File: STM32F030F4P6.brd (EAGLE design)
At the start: 17.8 x 27.9 mm, 11 parts, among them J3 455-1750-1-ND, U1 STM32F030F4P6, U2 CJA1117B-3.3-SOT89

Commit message: Made inline.
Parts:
- moved J2 26.2 mm to (2.54, 2.54), turned to 90 degrees
- moved J1 25.4 mm to (2.54, 50.8)
- moved U1 12.7 mm to (8.89, 26.7), turned to 270 degrees
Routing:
- net SWCLK: track 11.4 -> 0.00 mm
- net BOOT0: track 11.4 -> 0.00 mm
- net A5: track 11.4 -> 0.00 mm
- net A4: track 11.4 -> 0.00 mm
- net SWDIO: track 9.25 -> 0.00 mm
- net A6: track 9.25 -> 0.00 mm
- net OSC_IN: track 9.25 -> 0.00 mm
- net A3: track 9.25 -> 0.00 mm
- net OSC_OUT: track 7.36 -> 0.00 mm
- net A2: track 7.36 -> 0.00 mm
- net A7: track 7.29 -> 0.00 mm
- net A10: track 7.29 -> 0.00 mm
- net NRST: track 5.40 -> 0.00 mm
- net A1: track 5.40 -> 0.00 mm
- net A9: track 5.03 -> 0.00 mm
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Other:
- board size 17.8 x 27.9 mm -> 17.8 x 53.3 mm

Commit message: Added capacitors, resistors, diodes, LEDs, and J-Link connector.
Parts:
- added C2, C3, C4, C5, C6, C7: (no value), adafruit:C0603
- added D2: (no value), adafruit:SOD-123
- added J4: CORTEX_DEBUG_MINIMUM_PTH, SparkFun-Connectors:2X5-PTH-1.27MM
- added LED2: (no value), adafruit:CHIPLED_0603
- added R2, R3, R4, R5: (no value), adafruit:R0603
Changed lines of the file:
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@@
 <attribute name="VALUE" x="4.572" y="1.27" size="0.6096" layer="27" font="vector" ratio="20" rot="R90"/>
+</element>
+<element name="R2" library="adafruit" package="R0603" value="" x="-36.83" y="-3.81" smashed="yes">
+<attribute name="NAME" x="-37.719" y="-2.921" size="1.27" layer="25"/>
+<attribute name="VALUE" x="-37.719" y="-5.842" size="1.27" layer="27"/>
+</element>
+<element name="R3" library="adafruit" package="R0603" value="" x="-36.83" y="-7.62" smashed="yes">
+<attribute name="NAME" x="-37.719" y="-6.731" size="1.27" layer="25"/>
+<attribute name="VALUE" x="-37.719" y="-9.652" size="1.27" layer="27"/>
+</element>
+<element name="R4" library="adafruit" package="R0603" value="" x="-36.83" y="-11.43" smashed="yes">
+<attribute name="NAME" x="-37.719" y="-10.541" size="1.27" layer="25"/>
+<attribute name="VALUE" x="-37.719" y="-13.462" size="1.27" layer="27"/>
+</element>
+<element name="R5" library="adafruit" package="R0603" value="" x="-36.83" y="-15.24" smashed="yes">
+<attribute name="NAME" x="-37.719" y="-14.351" size="1.27" layer="25"/>
+<attribute name="VALUE" x="-37.719" y="-17.272" size="1.27" layer="27"/>
+</element>
+<element name="C2" library="adafruit" package="C0603" value="" x="-36.83" y="-19.05" smashed="yes">
+<attribute name="NAME" x="-37.719" y="-18.288" size="1.27" layer="25"/>
+<attribute name="VALUE" x="-37.719" y="-21.082" size="1.27" layer="27"/>
+</element>
+<element name="C3" library="adafruit" package="C0603" value="" x="-36.83" y="-22.86" smashed="yes">
+<attribute name="NAME" x="-37.719" y="-22.098" size="1.27" layer="25"/>
+<attribute name="VALUE" x="-37.719" y="-24.892" size="1.27" layer="27"/>
+</element>
+<element name="C4" library="adafruit" package="C0603" value="" x="-36.83" y="-26.67" smashed="yes">
+<attribute name="NAME" x="-37.719" y="-25.908" size="1.27" layer="25"/>
+<attribute name="VALUE" x="-37.719" y="-28.702" size="1.27" layer="27"/>
+</element>
+<element name="C5" library="adafruit" package="C0603" value="" x="-36.83" y="-30.48" smashed="yes">
+<attribute name="NAME" x="-37.719" y="-29.718" size="1.27" layer="25"/>
+<attribute name="VALUE" x="-37.719" y="-32.512" size="1.27" layer="27"/>
+</element>
+<element name="C6" library="adafruit" package="C0603" value="" x="-36.83" y="-34.29" smashed="yes">
+<attribute name="NAME" x="-37.719" y="-33.528" size="1.27" layer="25"/>
+<attribute name="VALUE" x="-37.719" y="-36.322" size="1.27" layer="27"/>
+</element>
+<element name="C7" library="adafruit" package="C0603" value="" x="-36.83" y="-38.1" smashed="yes">
+<attribute name="NAME" x="-37.719" y="-37.338" size="1.27" layer="25"/>
+<attribute name="VALUE" x="-37.719" y="-40.132" size="1.27" layer="27"/>
+</element>
+<element name="LED2" library="adafruit" package="CHIPLED_0603" value="" x="-36.83" y="-43.18" smashed="yes">
+<attribute name="NAME" x="-37.465" y="-44.45" size="1.27" layer="25" rot="R90"/>
+<attribute name="VALUE" x="-34.925" y="-44.45" size="1.27" layer="27" rot="R90"/>
+</element>
+<element name="D2" library="adafruit" package="SOD-123" value="" x="-35.56" y="-46.99" smashed="yes">
+<attribute name="NAME" x="-36.66" y="-45.99" size="0.4064" layer="25"/>
+<attribute name="VALUE" x="-36.66" y="-48.274" size="0.4064" layer="27"/>
+</element>
+<element name="J4" library="SparkFun-Connectors" package="2X5-PTH-1.27MM" value="CORTEX_DEBUG_MINIMUM_PTH" x="-35.56" y="-52.07" smashed="yes">
+<attribute name="NAME" x="-37.1348" y="-50.1396" size="0.6096" layer="25" font="vector" ratio="20"/>
+<attribute name="VALUE" x="-37.3888" y="-54.5338" size="0.6096" layer="27" font="vector" ratio="20"/>
 </element>
 </elements>

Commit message: Connected all components.
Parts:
- added C8: (no value), adafruit:C0603
- added FRAME1: FRAME-LETTER, SparkFun-Aesthetics:CREATIVE_COMMONS
- added J5: (no value), SparkFun-Connectors:1X02
- J1: device SparkFun-Connectors:1X10 -> SparkFun-Connectors:1X11
- moved J2 22.9 mm to (2.54, 25.4), turned to 270 degrees
- moved J1 2.54 mm to (2.54, 53.3)
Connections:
- new net N$1: J3.2, R1.1
- new net N$3: C6.1, R2.1, Y1.P$1
- new net N$5: D2.A, U2.2, U2.4
- new net N$7: LED1.C, R3.2
- new net N$8: LED2.C, R4.1
- new net VIN_2.4-3.6V: D1.A, J2.7
- new net VIN_5-30V: C1.1, J1.1, U2.3
- net A0: now also J1.7, J5.1, J5.2, LED2.A; no longer J1.6
- net A1: now also J1.8; no longer J1.7
- net A10: now also J2.6; no longer J2.3
- net A2: now also J1.9; no longer J1.8
- net A3: now also J1.10; no longer J1.9
- net A4: now also J1.11; no longer J1.10
- net A5: now also J2.1; no longer J2.10
- net A6: now also J2.2; no longer J2.9
- net A7: now also J2.3; no longer J2.8
- net A9: now also J2.5; no longer J2.4
- net B1: now also J2.4; no longer J2.7
- net BOOT0: now also J1.2, R1.2; no longer J1.1
- net GND: now also C1.2, C2.2, C3.2, C4.2, C5.2, C6.2, C7.2, C8.2, J2.8, J3.1, J4.3, J4.5, J4.9, R3.1, R4.2, S1.1, S1.2, U2.1; no longer J2.6
- net NRST: now also C7.1, J1.5, J4.10, S1.3, S1.4; no longer J1.4
- net OSC_IN: now also C5.1, J1.3, Y1.P$2; no longer J1.2
- net OSC_OUT: now also J1.4, R2.2; no longer J1.3
- net SWCLK: now also J2.10, J4.4; no longer J2.1
- net SWDIO: now also J2.9, J4.2; no longer J2.2
- net VDD: now also C2.1, C3.1, D1.C, D2.C, J3.3, J4.1, LED1.A, R5.1; no longer J2.5
- net VDDA: now also C4.1, C8.1, J1.6, R5.2; no longer J1.5
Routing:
- net A6: track 0.00 -> 5.38 mm
- net A5: track 0.00 -> 4.52 mm
- net A4: track 0.00 -> 4.52 mm
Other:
- board size 17.8 x 53.3 mm -> 17.8 x 55.9 mm

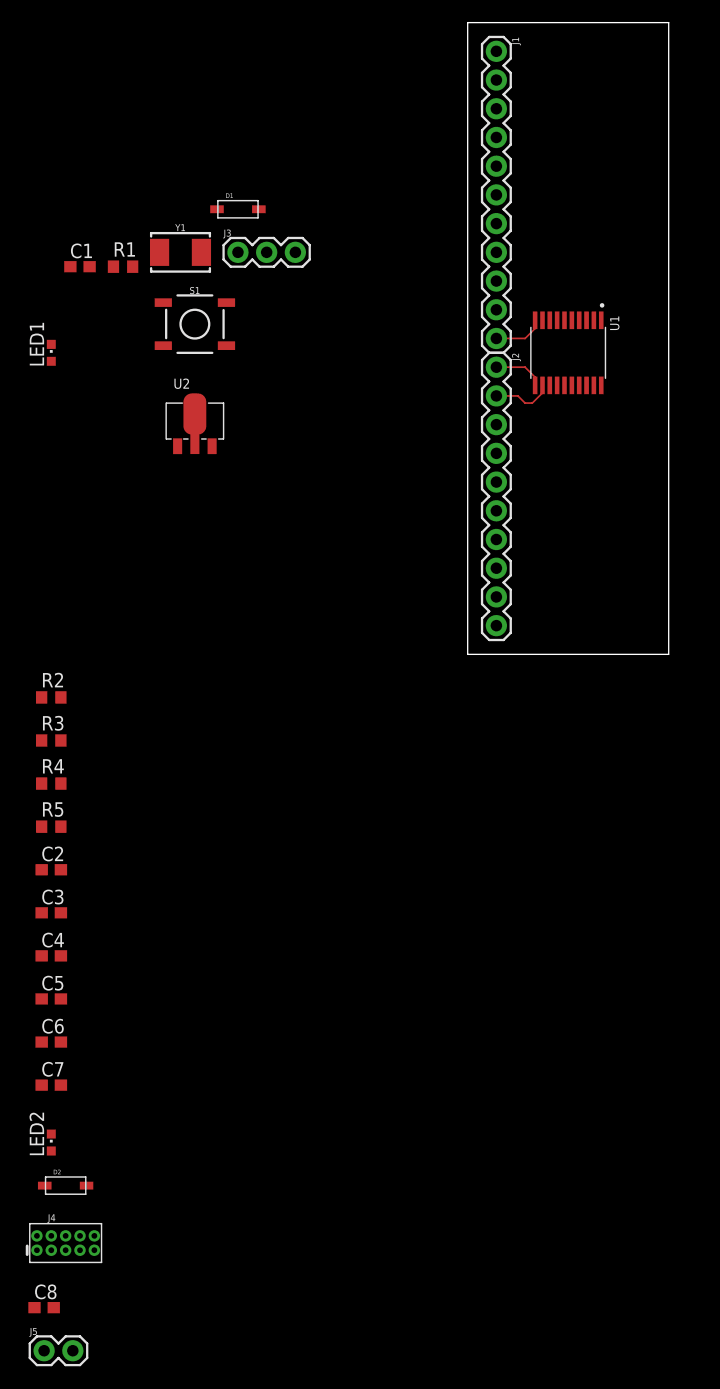
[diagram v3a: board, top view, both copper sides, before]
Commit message: Initial layout, placing VDD capacitors and HSE oscillator in close proximity to their respective pins.
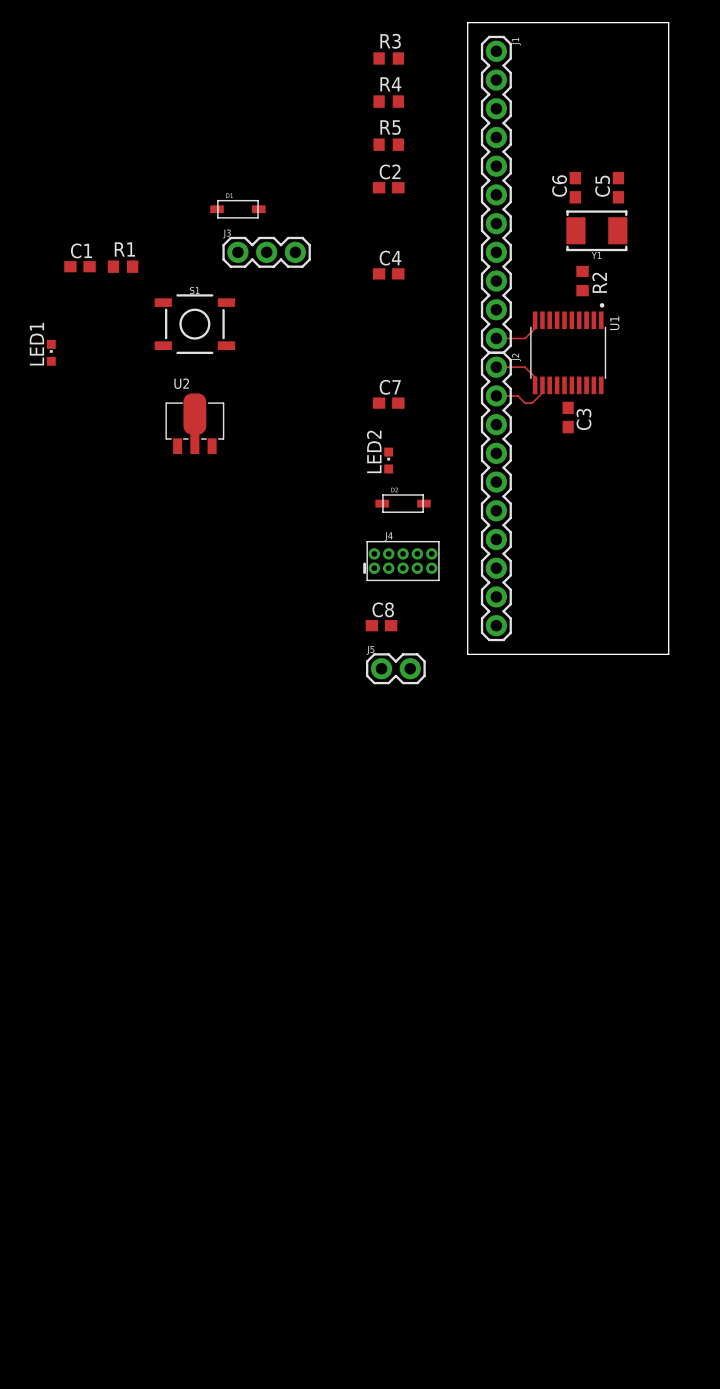
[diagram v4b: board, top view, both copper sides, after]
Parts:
- moved C6 88.7 mm to (9.53, 41.3), turned to 90 degrees
- moved C5 87.6 mm to (13.3, 41.3), turned to 90 degrees
- moved C2 67.3 mm to (-6.99, 41.3)
- moved C4 67.3 mm to (-6.99, 33.7)
- moved C7 67.3 mm to (-6.99, 22.2)
- moved D2 67.3 mm to (-5.71, 13.3)
- moved J4 67.3 mm to (-5.71, 8.26)
- moved LED2 67.3 mm to (-6.99, 17.1)
- moved R4 67.3 mm to (-6.99, 48.9)
- moved R5 67.3 mm to (-6.99, 45.1)
- moved C8 67.3 mm to (-7.62, 2.54)
- moved J5 67.3 mm to (-7.62, -1.27)
- moved R3 67.3 mm to (-6.99, 52.7)
- moved C3 63.3 mm to (8.89, 21.0), turned to 270 degrees
- moved R2 59.7 mm to (10.2, 33.0), turned to 270 degrees
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
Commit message: Initial placement. Added diode between VDD and VDDA. Added pulldown resistor to BOOT0.
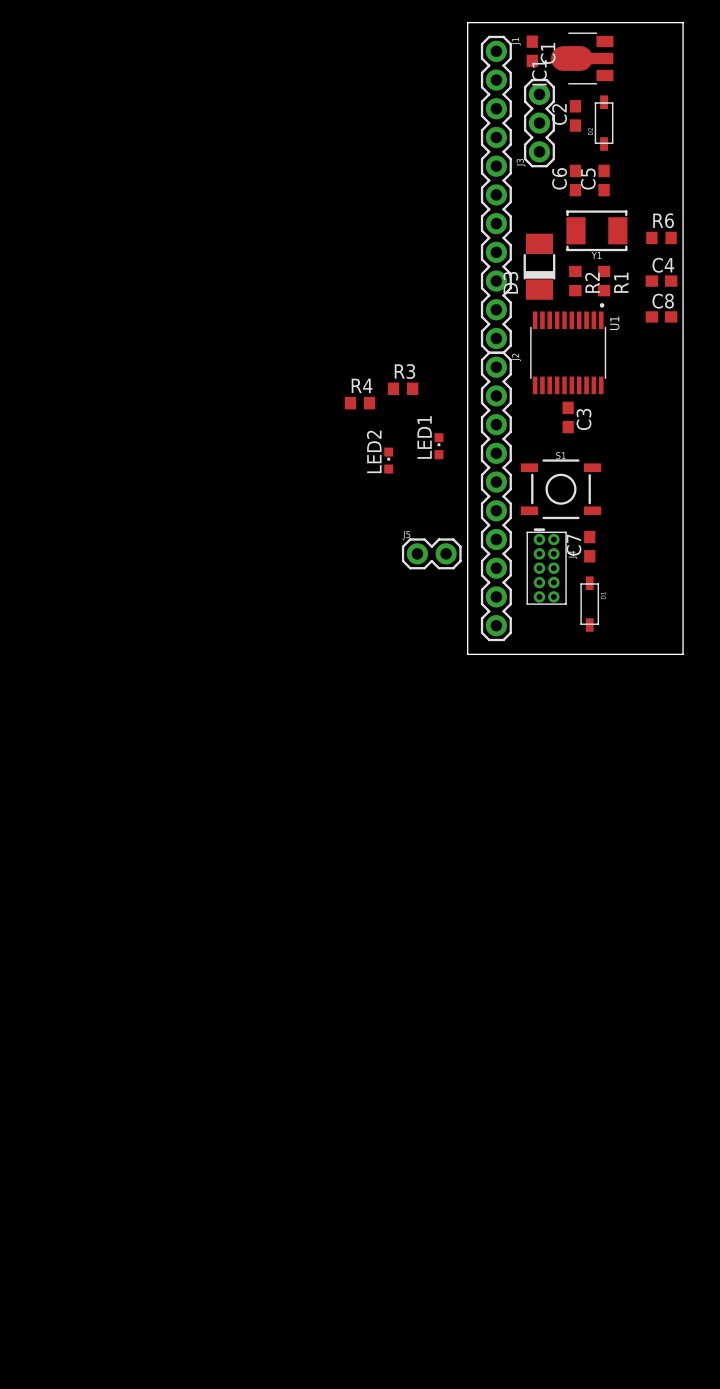
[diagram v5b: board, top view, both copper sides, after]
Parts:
- removed R5: (no value), adafruit:R0603
- removed U2: CJA1117B-3.3-SOT89, OPL_IC:SOT-89
- added D3: (no value), diode:DO-214AC
- added IC1: MCP170333MB, linear:SOT89
- added R6: (no value), adafruit:R0603
- moved FRAME1 96.8 mm to (45.1, 2.54)
- moved D1 46.8 mm to (10.8, 4.45), turned to 270 degrees
- moved C1 44.3 mm to (5.71, 53.3), turned to 270 degrees
- moved R1 42.6 mm to (12.1, 33.0), turned to 270 degrees
- moved D2 38.1 mm to (12.1, 47.0), turned to 90 degrees
- moved C8 36.9 mm to (17.1, 29.8)
- moved S1 35.5 mm to (8.26, 14.6)
- moved LED1 35.3 mm to (-2.54, 18.4)
- moved R3 29.2 mm to (-5.71, 23.5)
- moved J3 28.1 mm to (6.35, 44.5), turned to 90 degrees
- moved R4 26.8 mm to (-9.53, 22.2)
- moved C4 24.1 mm to (17.1, 33.0)
- moved C7 21.8 mm to (10.8, 9.53), turned to 90 degrees
- moved C2 17.7 mm to (9.53, 47.6), turned to 90 degrees
- moved J4 12.7 mm to (6.99, 7.62), turned to 270 degrees
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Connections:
- net A0: now also J1.6; no longer J1.7
- net A1: now also J1.7; no longer J1.8
- net A10: now also J2.5; no longer J2.6
- net A2: now also J1.8; no longer J1.9
- net A3: now also J1.9; no longer J1.10
- net A4: now also J1.10; no longer J1.11
- net A5: now also J1.11; no longer J2.1
- net A6: now also J2.1; no longer J2.2
- net A7: now also J2.2; no longer J2.3
- net A9: now also J2.4; no longer J2.5
- net B1: now also J2.3; no longer J2.4
- net GND: now also IC1.1, J2.9, R6.1; no longer J2.8, U2.1
- net N$1: now also R6.2
- net N$5: now also IC1.3; no longer U2.2, U2.4
- net NRST: now also J2.6; no longer J1.5
- net SWCLK: now also J2.8; no longer J2.10
- net SWDIO: now also J2.7; no longer J2.9
- net VDD: now also D3.A; no longer R5.1
- net VDDA: now also D3.C, J1.5; no longer J1.6, R5.2
- net VIN_2.4-3.6V: now also J2.10; no longer J2.7
- net VIN_5-30V: now also IC1.2@1; no longer U2.3
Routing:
- net A6: track 5.38 -> 0.00 mm
- net A5: track 4.52 -> 0.00 mm
- net A4: track 4.52 -> 0.00 mm
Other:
- board size 17.8 x 55.9 mm -> 19.1 x 55.9 mm

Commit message: Finished.
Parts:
- removed FRAME1: FRAME-LETTER, SparkFun-Aesthetics:CREATIVE_COMMONS
- removed J5: (no value), SparkFun-Connectors:1X02
- removed R6: (no value), adafruit:R0603
- added FRAME2: FRAME-LETTERNO_PACKAGE, SparkFun-Aesthetics:DUMMY
- added R5: 0R, adafruit:R0603
- C1: value (none) -> 10uF
- C2: value (none) -> 4.7uF
- C3, C8: value (none) -> 100nF
- C4: value (none) -> 1uF
- C5: value (none) -> 10nF
- C6, C7: value (none) -> 20pF
- J1: device SparkFun-Connectors:1X11 -> SparkFun-Connectors:1X19
- J2: value (none) -> 455-1750-1-ND; device SparkFun-Connectors:1X10 -> SparkFun-Connectors:1X03
- J3: value 455-1750-1-ND -> (none); device SparkFun-Connectors:1X03 -> SparkFun-Connectors:1X02
- R1, R2: value (none) -> 100R
- R3: value (none) -> 1k
- R4: value (none) -> 10k
- moved C1 50.9 mm to (9.53, 2.54), turned to 0 degrees
- moved IC1 49.1 mm to (14.6, 3.81)
- moved C2 41.9 mm to (9.53, 5.71), turned to 180 degrees
- moved D2 38.8 mm to (14.6, 8.26), turned to 0 degrees
- moved C7 35.3 mm to (15.9, 44.5)
- moved R4 28.7 mm to (15.9, 35.6), turned to 90 degrees
- moved J2 24.5 mm to (11.4, 48.3), turned to 0 degrees
- moved LED2 24.4 mm to (15.2, 27.3), turned to 270 degrees
- moved J3 23.9 mm to (15.2, 22.2)
- moved R3 21.5 mm to (12.1, 35.6), turned to 270 degrees
- moved LED1 20.8 mm to (15.2, 29.2), turned to 270 degrees
- moved R2 15.1 mm to (15.2, 19.1), turned to 180 degrees
- moved C8 9.44 mm to (10.8, 22.9), turned to 90 degrees
- moved C4 9.09 mm to (8.26, 34.9), turned to 180 degrees
- moved D3 8.47 mm to (8.26, 42.5)
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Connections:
- removed net N$8: LED2.C, R4.1
- new net N$2: J3.1, J3.2, LED2.C, R2.1
- net A0: now also J1.3; no longer J1.6, J5.1, J5.2
- net A1: now also J1.4; no longer J1.7
- net A10: now also J1.13; no longer J2.5
- net A2: now also J1.5; no longer J1.8
- net A3: now also J1.6; no longer J1.9
- net A4: now also J1.7; no longer J1.10
- net A5: now also J1.8; no longer J1.11
- net A6: now also J1.9; no longer J2.1
- net A7: now also J1.10; no longer J2.2
- net A9: now also J1.12; no longer J2.4
- net B1: now also J1.11; no longer J2.3
- net BOOT0: now also J1.1, R4.2; no longer J1.2, R1.2
- net GND: now also J1.17, J2.1, R1.1, R2.2, R5.1; no longer J2.9, J3.1, R3.1, R4.2, R6.1
- net N$1: now also J2.2, R4.1, R5.2; no longer J3.2, R1.1, R6.2
- net N$3: now also R3.1; no longer R2.1
- net N$7: now also R1.2; no longer R3.2
- net NRST: now also C8.1, J1.14; no longer C7.1, J2.6
- net OSC_IN: now also C7.1; no longer C5.1, J1.3
- net OSC_OUT: now also R3.2; no longer J1.4, R2.2
- net SWCLK: now also J1.16; no longer J2.8
- net SWDIO: now also J1.15; no longer J2.7
- net VDD: now also J2.3; no longer J3.3
- net VDDA: now also C5.1, J1.2; no longer C8.1, J1.5
- net VIN_2.4-3.6V: now also J1.18; no longer J2.10
- net VIN_5-30V: now also J1.19; no longer J1.1
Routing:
- net NRST: track 0.00 -> 48.1 mm, vias 0 -> 1
- net BOOT0: track 0.00 -> 32.1 mm
- net SWCLK: track 0.00 -> 26.0 mm
- net A0: track 0.00 -> 24.0 mm, vias 0 -> 1
- net N$1: track 0.00 -> 23.7 mm
- net SWDIO: track 0.00 -> 23.3 mm
- net VDD: track 0.00 -> 19.7 mm, vias 0 -> 5
- net VDDA: track 0.00 -> 17.5 mm
- net OSC_IN: track 0.00 -> 13.8 mm
- net A10: track 0.00 -> 13.7 mm
- net VIN_5-30V: track 0.00 -> 11.7 mm
- net A9: track 0.00 -> 11.6 mm
- net A1: track 0.00 -> 11.2 mm
- net N$2: track 0.00 -> 8.92 mm
- net A2: track 0.00 -> 8.34 mm
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- added copper zone on layer 1, net GND
- added copper zone on layer 16, net VDD
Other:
- board size 19.1 x 55.9 mm -> 19.1 x 50.8 mm
- board text added: "(A0)"
- board text added: "<0> BOOT0 <1>"
- board text added: "A0"
- board text added: "A1"
- board text added: "A10"
- board text added: "A2"
- board text added: "A3"
- board text added: "A4"
- board text added: "A5"
- board text added: "A6"
- board text added: "A7"
- board text added: "A9"
- board text added: "B1"
- board text added: "BOOT0"
- board text added: "CLK"
- board text added: "DIO"
- board text added: "FMI: github.com/nathancharlesjones/Embedded-for-Everyone/wiki"
- board text added: "GND"
- board text added: "J-Link"
- board text added: "NRST"
- board text added: "PWR"
- board text added: "ST-Link"
- board text added: "USER"
- board text added: "VDDA"
- board text added: "VIN, 2.4-3.6V: MCU damage may occur if >4V Max current, ea pin: 25 mA Mx current, all pins: 80 mA USER LED on A0 (pin 6); Cut trace btwn J3 on TOP of PCB to remove LED (in- stall jumper to reinsert) -------------------- U1: STM32F030F4P6 IC1: 2.4-3.6V regulator, >=100mA / SOT-89-3 (ex: LCSC part# C14289) Y1: 8MHz re sonator / 5x 3.2mm (ex: LCSC part# C115962) J2: J-Link connector (ex: HPH2-A-10-U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"
- board text added: "VIN: 2.4 -3.6V"
- board text added: "VIN: 5- 30V"
